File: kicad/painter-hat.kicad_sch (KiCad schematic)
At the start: 21 parts, among them J1 Conn_01x08_Socket, J2 Conn_01x08_Socket, J3 Conn_01x08_Socket, J4 Conn_01x08_Socket, J5 Conn_02x20_Odd_Even, Q1 NPN, Q2 NPN, U1 MAX26405AFOAY+T, Y2 16 MHz

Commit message: finalized pcb
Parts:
- added H1, H2, H3, H4: MountingHole_Pad, MountingHole:MountingHole_2.7mm_M2.5_DIN965_Pad_TopBottom, symbol Mechanical:MountingHole_Pad
- added J6, J9: Conn_01x04, Connector_JST:JST_XH_B4B-XH-AM_1x04_P2.50mm_Vertical, symbol Connector_Generic:Conn_01x04
- C5, C6, C7: value C -> 22uF; footprint Capacitor_SMD:C_0603_1608Metric -> Capacitor_SMD:C_0805_2012Metric
- L1: value 1-2uH -> 3.3-4.7uH; footprint (none) -> Inductor_SMD:L_Coilcraft_XxL4030
- Q1, Q2: footprint (none) -> Package_TO_SOT_THT:TO-92L_Inline_Wide
- U1: footprint Package_DFN_QFN:FC2QFN-17 -> Own:FC2QFN-17
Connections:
- net Config 3_3 is gone; now on net Config 2_3: J4.4 (Pin_4)
- net Sleep 1 is gone; now on net Config 1_4: J2.5 (Pin_5)
- net Sleep 2 is gone; now on net Config 2_4: J4.5 (Pin_5)
- net Config 1_1: now also J5.36 (Pin_36)
- net Config 1_2: now also J5.11 (Pin_11)
- net Config 1_3: now also J5.38 (Pin_38)
- net Config 2_1: now also J5.40 (Pin_40)
- net Config 2_2: now also J5.15 (Pin_15)
- net GND: now also H1.1, H2.1, H3.1, H4.1; no longer U1.4 (PGND), U1.8 (PGND)
- net Motor1_A: now also J6.4 (Pin_4)
- net Motor1_B: now also J6.3 (Pin_3)
- net Motor2_A: now also J6.2 (Pin_2)
- net Motor2_B: now also J6.1 (Pin_1)
- net Motor3_A: now also J9.4 (Pin_4)
- net Motor3_B: now also J9.3 (Pin_3)
- net Motor4_A: now also J9.2 (Pin_2)
- net Motor4_B: now also J9.1 (Pin_1)
- net Config 2_3: now reaches J5.13 (Pin_13)
- net Config 2_4: now reaches J5.31 (Pin_31)
- net Config 1_4: now reaches J5.37 (Pin_37)

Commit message: feat: v2
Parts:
- removed L1: 3.3-4.7uH, Inductor_SMD:L_Coilcraft_XxL4030, symbol Device:L
- removed Q1, Q2: NPN, Package_TO_SOT_THT:TO-92L_Inline_Wide, symbol Simulation_SPICE:NPN
- removed R1, R2, R3, R4: R, Resistor_SMD:R_0603_1608Metric, symbol Device:R
- removed U1: MAX26405AFOAY+T, Own:FC2QFN-17, symbol Own:MAX26405AFOAY+T
- added C19, C20, C21: 10nF, Capacitor_SMD:C_0402_1005Metric, symbol Device:C
- added J7: Conn_01x06, Connector_PinSocket_2.54mm:PinSocket_1x06_P2.54mm_Vertical, symbol Connector_Generic:Conn_01x06
- added R14: 10k, Resistor_SMD:R_0402_1005Metric, symbol Device:R
- added SW1, SW2: SW_Push, Button_Switch_SMD:SW_Push_1P1T_NO_CK_KMR2, symbol Switch:SW_Push
- added U4: STM32F103CB, Package_QFP:LQFP-48_7x7mm_P0.5mm, symbol MCU_ST_STM32F1:STM32F103CBTx
- C1: value 12uF -> 4.7uF; footprint Capacitor_SMD:C_0603_1608Metric -> Capacitor_SMD:C_0402_1005Metric
- C2, C3: value 4.7uF -> 100nF; footprint Capacitor_SMD:C_0603_1608Metric -> Capacitor_SMD:C_0402_1005Metric
- C4: value 2.2uF -> 100nF; footprint Capacitor_SMD:C_0603_1608Metric -> Capacitor_SMD:C_0402_1005Metric
- C5, C6: value 22uF -> 100nF; footprint Capacitor_SMD:C_0805_2012Metric -> Capacitor_SMD:C_0402_1005Metric
- C7: value 22uF -> 1uF; footprint Capacitor_SMD:C_0805_2012Metric -> Capacitor_SMD:C_0603_1608Metric
- J1, J2, J3, J4: footprint Connector_PinHeader_2.54mm:PinHeader_1x08_P2.54mm_Vertical -> Connector_PinSocket_2.54mm:PinSocket_1x08_P2.54mm_Vertical
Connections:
- net +5V: no longer C5.2, C6.2, C7.2
- net Direction 1: now also U4.46 (PB9); no longer J5.33 (Pin_33)
- net Direction 2: now also U4.18 (PB0); no longer J5.18 (Pin_18)
- net Enable 1: now also J2.1 (Pin_1), U4.39 (PB3); no longer J5.32 (Pin_32)
- net Enable 2: now also J4.1 (Pin_1), U4.27 (PB14); no longer J5.7 (Pin_7)
- net GND: now also C1.2, C3.2, C5.2, C6.2, C7.2, C19.2, C20.2, C21.2, J7.2 (Pin_2), J7.6 (Pin_6), SW1.1, U4.23 (VSS), U4.35 (VSS), U4.47 (VSS), U4.8 (VSSA); no longer C3.1, C5.1, C6.1, C7.1, J5.14 (Pin_14), J5.20 (Pin_20), J5.25 (Pin_25), J5.30 (Pin_30), J5.34 (Pin_34), J5.39 (Pin_39)
- net Step 1: now also U4.45 (PB8); no longer J5.35 (Pin_35)
- net Step 2: now also U4.19 (PB1); no longer J5.12 (Pin_12)
- net SPI1_MOSI: now reaches J5.19 (Pin_19)
- net SPI1_MOSI: now also U4.17 (PA7)
- net SPI1_MISO: now reaches J5.21 (Pin_21)
- net SPI1_MISO: now also U4.16 (PA6)
- net SPI1_SCK: now reaches J5.23 (Pin_23)
- net SPI1_SCK: now also U4.15 (PA5)
- net VDD: now reaches C2.1
- net VDD: now also C1.1, C3.1, C4.1, C5.1, C6.1, C7.1, C19.1, J7.1 (Pin_1), R14.1, SW2.1, U4.24 (VDD), U4.36 (VDD), U4.48 (VDD)
- net Config 1_1: no longer names the net of J5.36 (Pin_36)
- net Config 1_1: no longer J2.2 (Pin_2)
- net Config 1_2: no longer names the net of J5.11 (Pin_11)
- net Config 1_2: no longer J2.3 (Pin_3)
- net Config 1_3: no longer names the net of J5.38 (Pin_38)
- net Config 1_3: no longer J2.4 (Pin_4)
- net Config 1_4: no longer names the net of J5.37 (Pin_37)
- net Config 1_4: no longer J2.5 (Pin_5)
- net Config 2_1: no longer names the net of J5.40 (Pin_40)
- net Config 2_1: no longer J4.2 (Pin_2)
- net Config 2_2: no longer names the net of J5.15 (Pin_15)
- net Config 2_2: no longer J4.3 (Pin_3)
- net Config 2_3: no longer names the net of J5.13 (Pin_13)
- net Config 2_3: no longer J4.4 (Pin_4)
- net Config 2_4: no longer names the net of J5.31 (Pin_31)
- net Config 2_4: no longer J4.5 (Pin_5)
- new net: SW2.2, U4.44 (BOOT0)
- new net I2C1_SCL: U4.42 (PB6)
- new net I2C1_SDA: U4.43 (PB7)
- new net MS 1_1: J2.2 (Pin_2), U4.40 (PB4)
- new net MS 1_2: J2.3 (Pin_3), U4.41 (PB5)
- new net MS 2_1: J4.2 (Pin_2), U4.26 (PB13)
- new net MS 2_2: J4.3 (Pin_3), U4.25 (PB12)
- new net NRST: J7.5 (Pin_5), R14.2, SW1.2, U4.7 (NRST)
- new net SPI1_~{SS}: U4.14 (PA4)
- new net SWCLK: J7.4 (Pin_4), U4.37 (PA14)
- new net SWDIO: J7.3 (Pin_3), U4.34 (PA13)
- new net UART1_RX: U4.31 (PA10)
- new net UART1_TX: U4.30 (PA9)
- new net UART2_RX: J2.5 (Pin_5), U4.13 (PA3)
- new net UART2_TX: J2.4 (Pin_4), U4.12 (PA2)
- new net UART3_RX: J4.5 (Pin_5), U4.22 (PB11)
- new net UART3_TX: J4.4 (Pin_4), U4.21 (PB10)
- new net VDDA: C20.1, C21.1, U4.9 (VDDA)
- new net ~{HP INT}: U4.28 (PB15)
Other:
- note added: "4.7uF has to be at Vdd3"
- note added: "removed bat because of space constraints"
- moved on the sheet: H1, H2, H3, H4, J1, J2, J3, J4, J5, J6, J9, Y2

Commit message: fix: minor additions to v2
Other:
- company: (none) -> vividsystem
- title: (none) -> Painter HAT Main Sheet
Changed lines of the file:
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@@
 	(generator_version "9.0")
 	(paper "A4")
+	(title_block
+		(title "Painter HAT Main Sheet")
+		(rev "v2")
+		(company "vividsystem")
+	)
 	(text "4.7uF has to be at Vdd3\n"
 		(exclude_from_sim no)

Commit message: feat: v2.1
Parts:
- added C27, C28, C30, C31: 100uF, Capacitor_SMD:C_Elec_8x10.2, symbol Device:C
- C1: footprint Capacitor_SMD:C_0402_1005Metric -> Capacitor_SMD:C_0603_1608Metric
- C7: footprint Capacitor_SMD:C_0603_1608Metric -> Capacitor_SMD:C_0402_1005Metric
- renumbered Y2 to Y1
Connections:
- net +5V: no longer Y1.1 (EN), Y1.4 (V+)
- net CLK 1: now also U4.3 (PC14)
- net Direction 1: now also U4.19 (PB1); no longer U4.46 (PB9)
- net Direction 2: now also U4.40 (PB4); no longer U4.18 (PB0)
- net Enable 1: now also U4.41 (PB5); no longer U4.39 (PB3)
- net GND: now also C27.2, C28.2, C30.2, C31.2
- net MS 1_1: now also U4.45 (PB8); no longer U4.40 (PB4)
- net MS 1_2: now also U4.46 (PB9); no longer U4.41 (PB5)
- net Step 1: now also U4.18 (PB0); no longer U4.45 (PB8)
- net Step 2: now also U4.39 (PB3); no longer U4.19 (PB1)
- net VD: now also C27.1, C28.1, C30.1, C31.1
- net VDD: now also Y1.1 (EN), Y1.4 (V+)
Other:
- moved on the sheet: J3, J4

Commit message: feat: updated everything
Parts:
- removed C27, C28, C30, C31: 100uF, Capacitor_SMD:C_Elec_8x10.2, symbol Device:C
- added C27, C28, C30, C31: 100uF, Capacitor_SMD:C_Elec_8x10.2, symbol Device:C_Polarized
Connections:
- net GND: now also C27.2, C28.2, C30.2, C31.2
- net VD: now also C27.1, C28.1, C30.1, C31.1

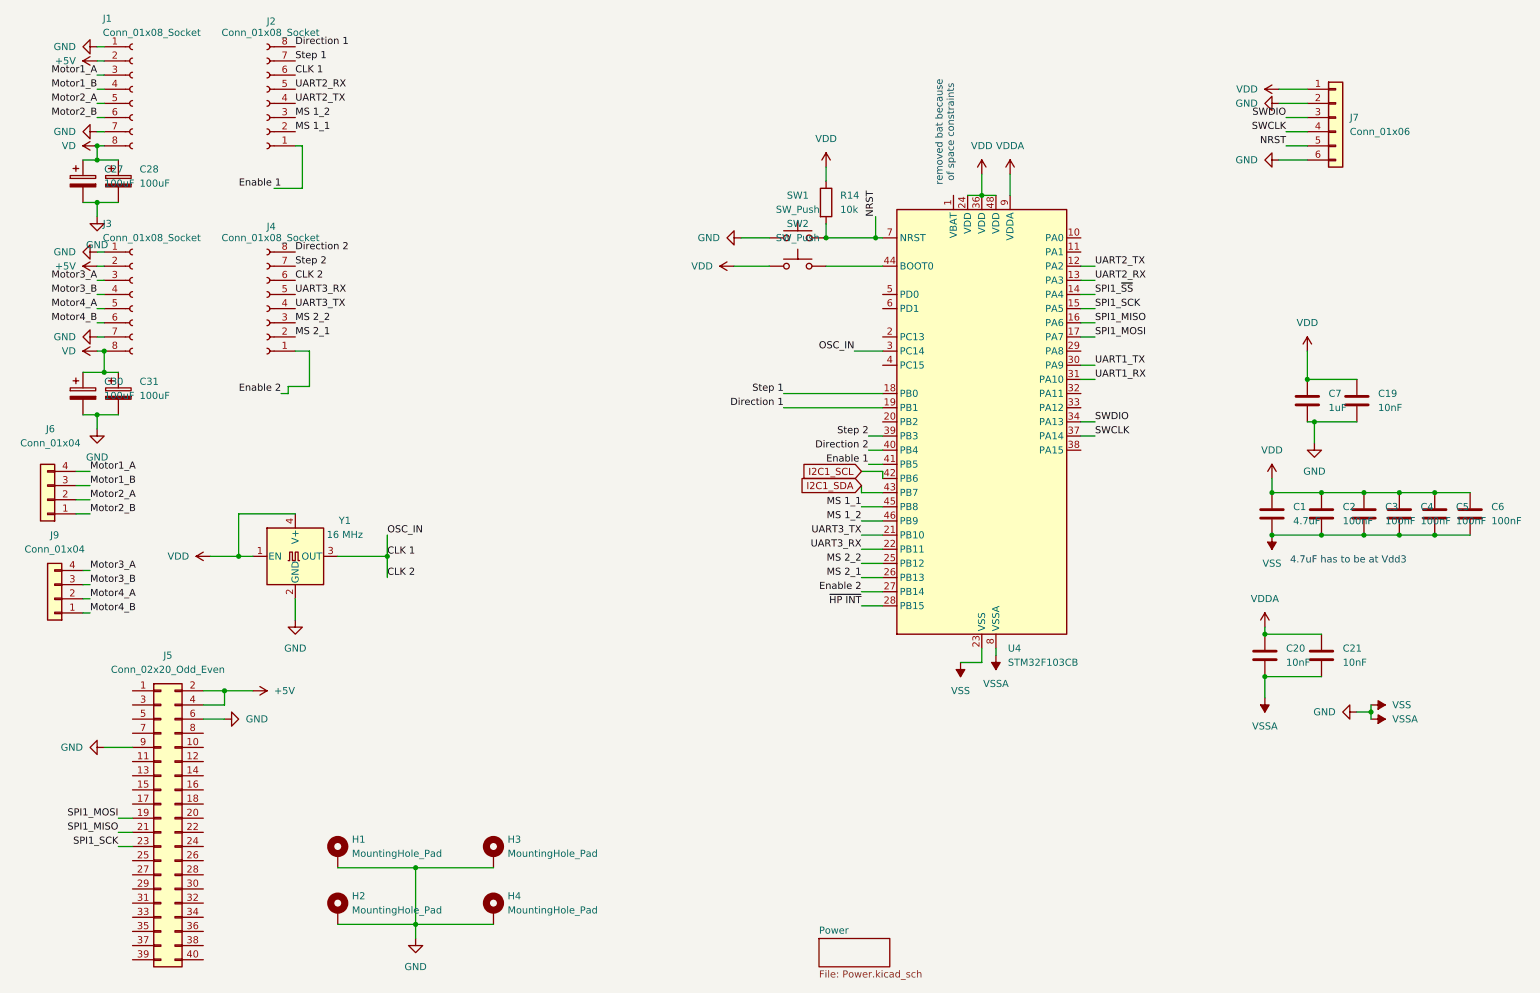
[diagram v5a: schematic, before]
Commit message: feat(v2.1.1): BOOT0, NRST Wiring, Polarized Caps fixed
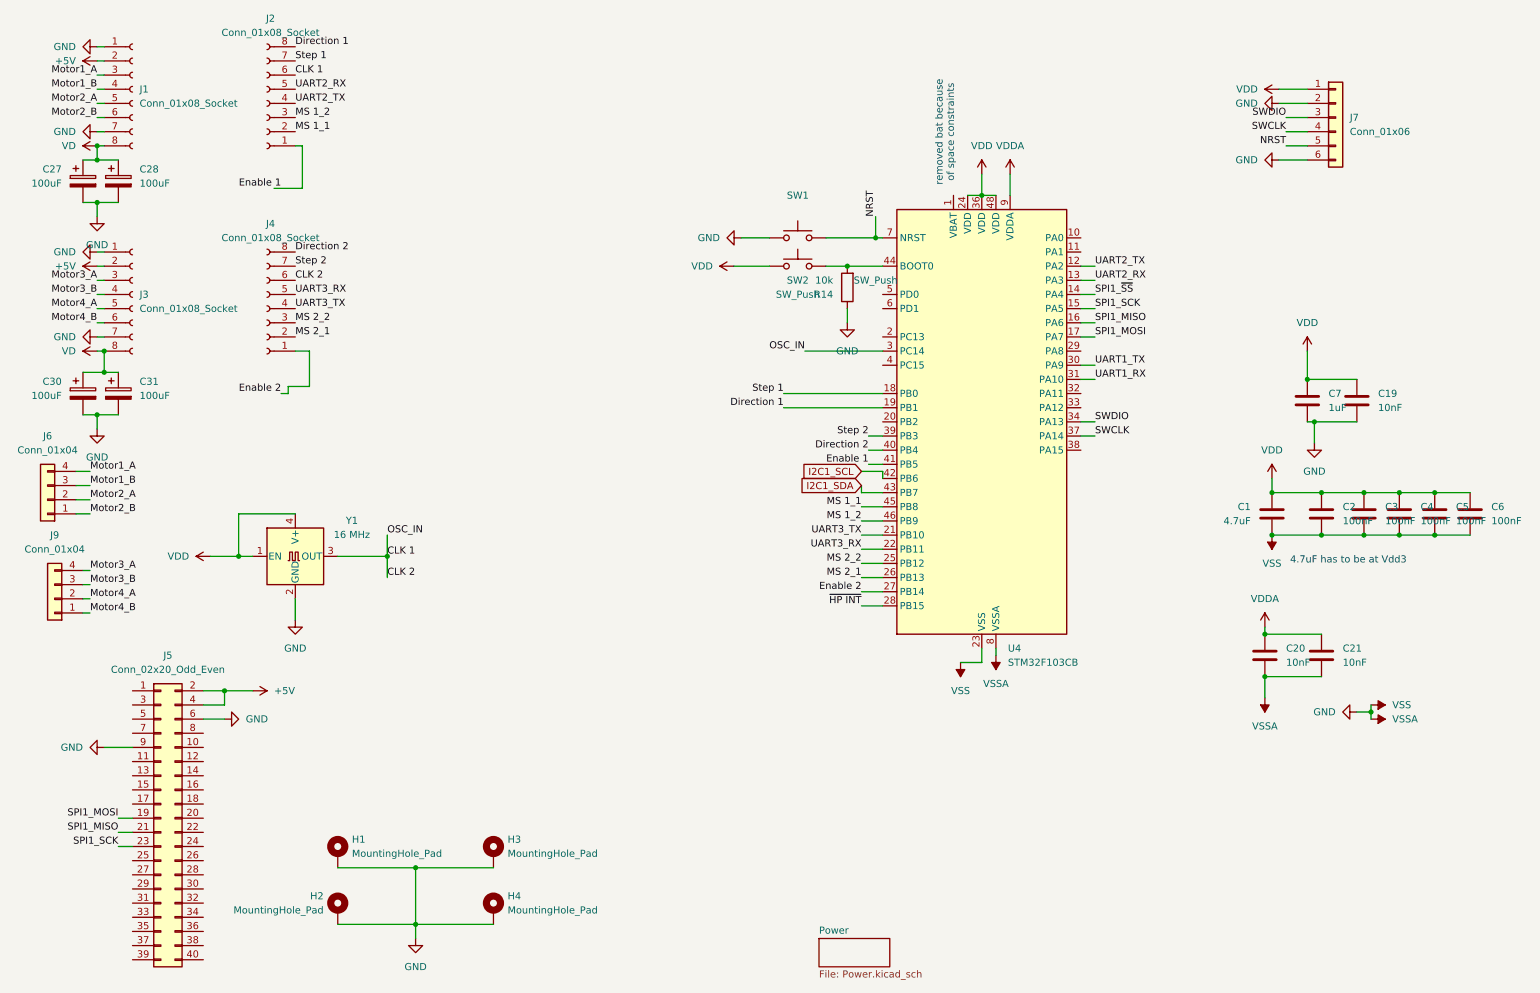
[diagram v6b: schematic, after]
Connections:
- net GND: now also R14.1
- net NRST: no longer R14.2
- net VDD: no longer R14.1
- net at SW2.2, U4.44 (BOOT0): now also R14.2
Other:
- moved on the sheet: R14
